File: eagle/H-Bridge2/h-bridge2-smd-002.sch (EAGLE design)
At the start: 29 parts

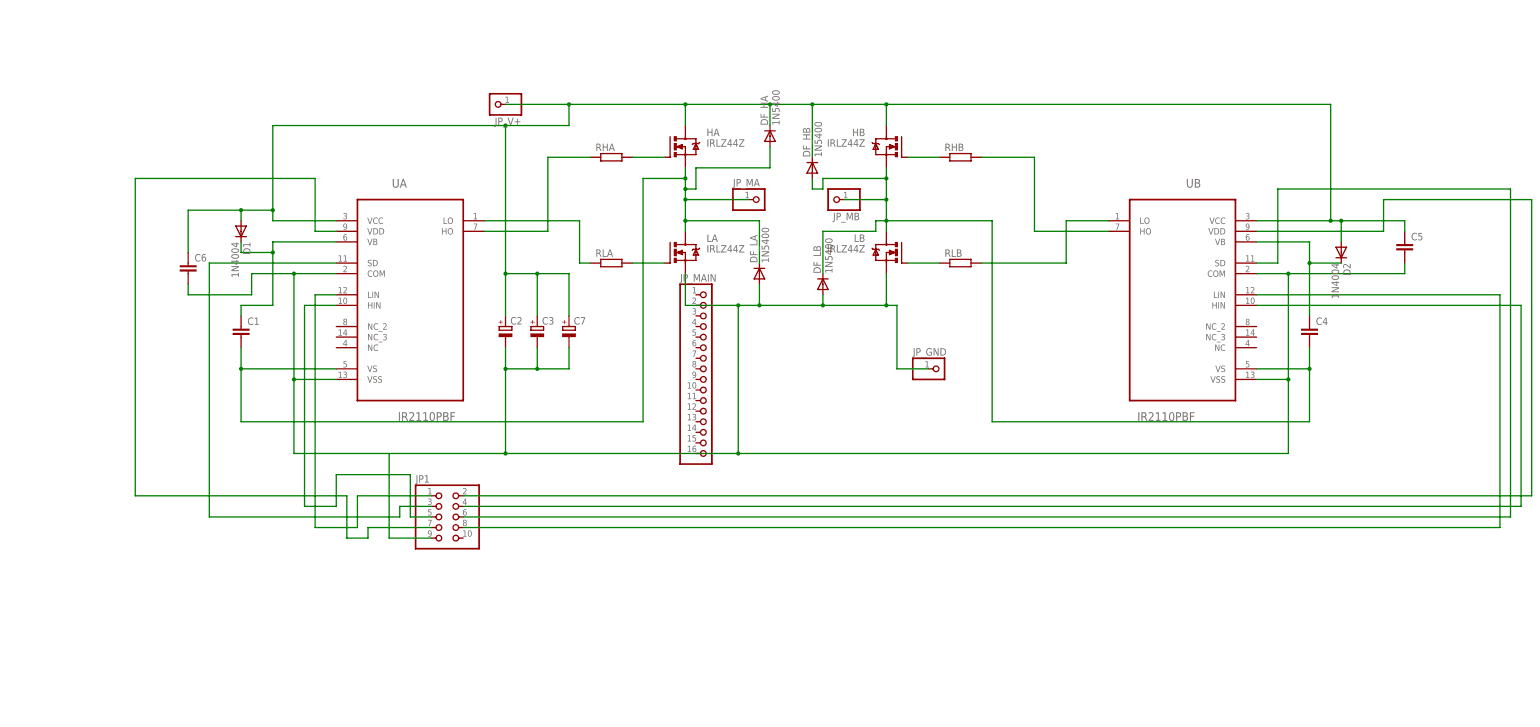
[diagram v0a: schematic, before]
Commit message: eagle merge template board with h-br
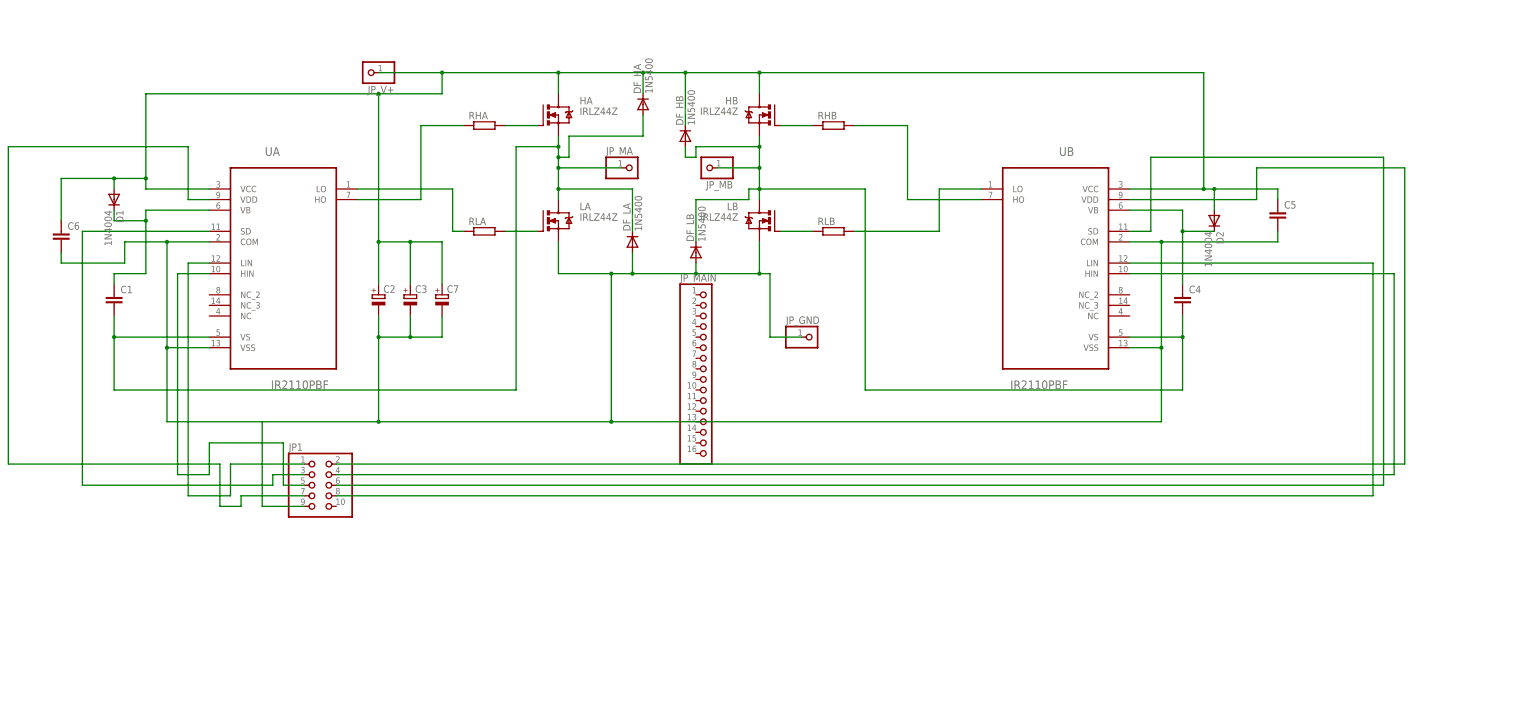
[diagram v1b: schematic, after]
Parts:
- RLA: device rcl:R-EU_0411/15 -> rcl:R-EU_R0603
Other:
- moved on the sheet: C1, C2, C3, C4, C5, C6, C7, D1, D2, DF_HA, DF_HB, DF_LA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

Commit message: H-bridge on SMD
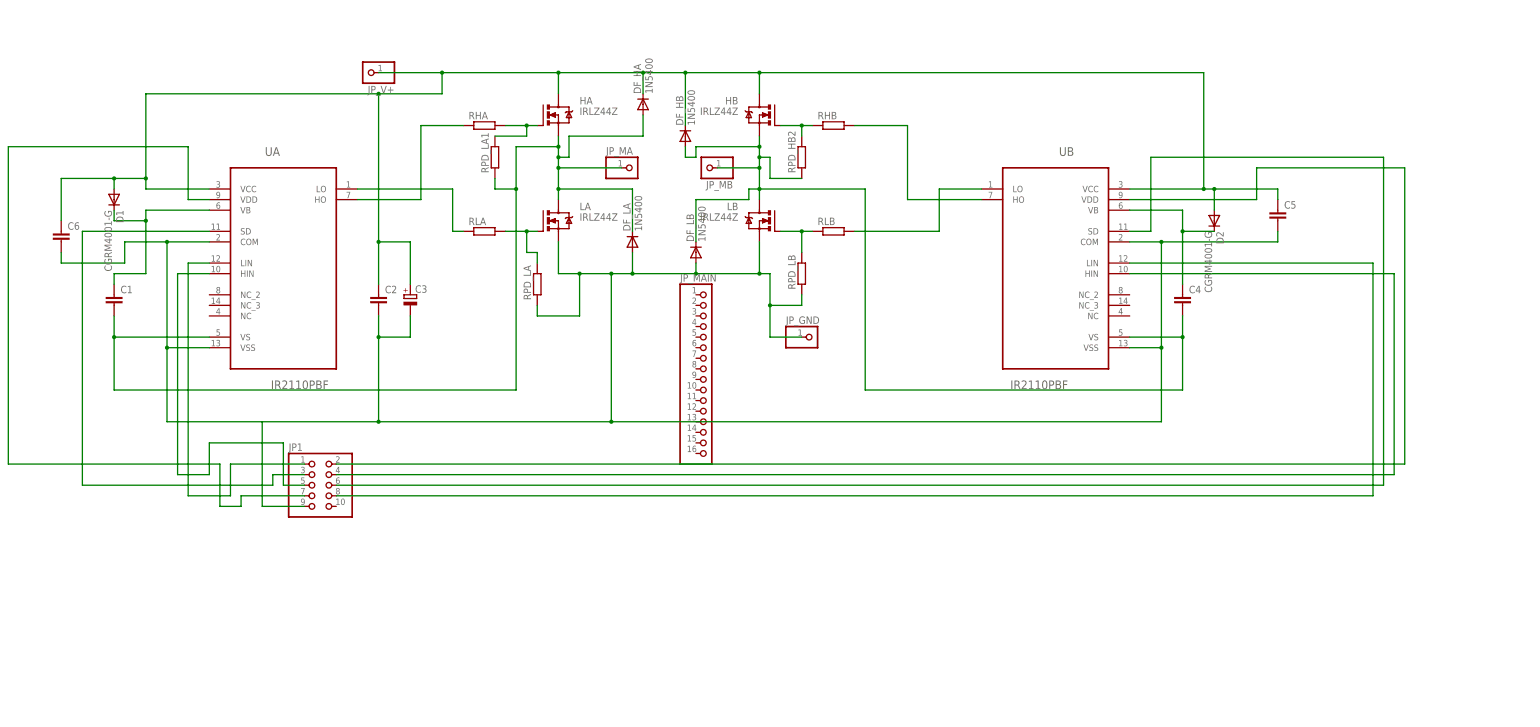
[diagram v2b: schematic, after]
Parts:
- removed C7: (no value), rcl:CPOL-EUE5-13
- added RPD_HB2, RPD_LA, RPD_LA1, RPD_LB: (no value), rcl:R-EU_R1206
- C1, C4, C5, C6: device rcl:C-EU025-025X050 -> rcl:C-EUC4532
- C2: device rcl:CPOL-EUE5-13 -> rcl:C-EU025-024X044
- D1, D2: value 1N4004 -> CGRM4001-G; device diode:1N4004 -> diode:CGRM4001-G
- RHA, RHB, RLB: device rcl:R-EU_0411/15 -> rcl:R-EU_R1206
- RLA: device rcl:R-EU_R0603 -> rcl:R-EU_R1206
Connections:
- net N$13: now also C2.1; no longer C2.+, C7.+
- net N$16: now also RPD_HB2.1
- net N$17: now also RPD_LA1.1
- net N$4: now also C2.2, RPD_LA.1, RPD_LB.1; no longer C2.-, C7.-
- net N$5: now also RPD_LA.2
- net N$6: now also RPD_LA1.2
- net N$7: now also RPD_HB2.2
- net N$8: now also RPD_LB.2

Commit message: H-bridge smd
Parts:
- removed C2: (no value), rcl:C-EU025-024X044
- added C7, C8: (no value), rcl:C-EUC4532
- added C9: (no value), rcl:CPOL-EUE5-13
- added JP_GND1, JP_V+1: (no value), dbg-misc:PINHD-1X1
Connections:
- net N$13: now also C7.1, C8.1, C9.+, JP_V+1.1; no longer C2.1
- net N$4: now also C7.2, C8.2, C9.-, JP_GND1.1; no longer C2.2
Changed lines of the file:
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@@
 <part name="DF_LB" library="dbg-misc" deviceset="1N5400" device=""/>
 <part name="DF_LA" library="dbg-misc" deviceset="1N5400" device=""/>
-<part name="C2" library="rcl" deviceset="C-EU" device="025-024X044"/>
 <part name="C3" library="rcl" deviceset="CPOL-EU" device="E5-13"/>
 <part name="RPD_LB" library="rcl" deviceset="R-EU_" device="R1206"/>
@@
 <part name="RPD_LA1" library="rcl" deviceset="R-EU_" device="R1206"/>
 <part name="RPD_HB2" library="rcl" deviceset="R-EU_" device="R1206"/>
+<part name="C7" library="rcl" deviceset="C-EU" device="C4532"/>
+<part name="C8" library="rcl" deviceset="C-EU" device="C4532"/>
+<part name="C9" library="rcl" deviceset="CPOL-EU" device="E5-13"/>
+<part name="JP_V+1" library="dbg-misc" deviceset="PINHD-1X1" device=""/>
+<part name="JP_GND1" library="dbg-misc" deviceset="PINHD-1X1" device=""/>
 </parts>
 <sheets>
@@
 <instance part="DF_LB" gate="1" x="10.16" y="78.74" rot="R90"/>
 <instance part="DF_LA" gate="1" x="-5.08" y="81.28" rot="R90"/>
-<instance part="C2" gate="G$1" x="-66.04" y="68.58"/>
 <instance part="C3" gate="G$1" x="-58.42" y="68.58"/>
 <instance part="RPD_LB" gate="G$1" x="35.56" y="73.66" rot="R90"/>
@@
 <instance part="RPD_LA1" gate="G$1" x="-38.1" y="101.6" rot="R90"/>
 <instance part="RPD_HB2" gate="G$1" x="35.56" y="101.6" rot="R90"/>
+<instance part="C7" gate="G$1" x="-66.04" y="68.58"/>
+<instance part="C8" gate="G$1" x="-50.8" y="68.58"/>
+<instance part="C9" gate="G$1" x="-43.18" y="68.58"/>
+<instance part="JP_V+1" gate="G$1" x="-68.58" y="134.62" rot="R180"/>
+<instance part="JP_GND1" gate="G$1" x="38.1" y="48.26"/>
 </instances>
 <busses>
@@
 <junction x="10.16" y="73.66"/>
 <junction x="-5.08" y="73.66"/>
-<pinref part="C2" gate="G$1" pin="2"/>
 <wire x1="-66.04" y1="63.5" x2="-66.04" y2="58.42" width="0.1524" layer="91"/>
 <junction x="-66.04" y="38.1"/>
@@
 <wire x1="35.56" y1="66.04" x2="27.94" y2="66.04" width="0.1524" layer="91"/>
 <junction x="27.94" y="66.04"/>
+<pinref part="C7" gate="G$1" pin="2"/>
+<pinref part="C9" gate="G$1" pin="-"/>
+<wire x1="-58.42" y1="58.42" x2="-50.8" y2="58.42" width="0.1524" layer="91"/>
+<wire x1="-50.8" y1="58.42" x2="-43.18" y2="58.42" width="0.1524" layer="91"/>
+<wire x1="-43.18" y1="58.42" x2="-43.18" y2="63.5" width="0.1524" layer="91"/>
+<pinref part="C8" gate="G$1" pin="2"/>
+<wire x1="-50.8" y1="63.5" x2="-50.8" y2="58.42" width="0.1524" layer="91"/>
+<junction x="-50.8" y="58.42"/>
+<pinref part="JP_GND1" gate="G$1" pin="1"/>
+<wire x1="35.56" y1="48.26" x2="27.94" y2="48.26" width="0.1524" layer="91"/>
+<wire x1="27.94" y1="48.26" x2="27.94" y2="58.42" width="0.1524" layer="91"/>
+<junction x="27.94" y="58.42"/>
 </segment>
 </net>
@@
 <wire x1="-66.04" y1="121.92" x2="-50.8" y2="121.92" width="0.1524" layer="91"/>
 <pinref part="HB" gate="G$1" pin="D"/>
-<wire x1="-50.8" y1="121.92" x2="-22.86" y2="121.92" width="0.1524" layer="91"/>
+<wire x1="-50.8" y1="121.92" x2="-43.18" y2="121.92" width="0.1524" layer="91"/>
+<wire x1="-43.18" y1="121.92" x2="-22.86" y2="121.92" width="0.1524" layer="91"/>
 <wire x1="-22.86" y1="121.92" x2="-2.54" y2="121.92" width="0.1524" layer="91"/>
 <wire x1="-2.54" y1="121.92" x2="7.62" y2="121.92" width="0.1524" layer="91"/>
@@
 <junction x="-2.54" y="121.92"/>
 <junction x="7.62" y="121.92"/>
-<pinref part="C2" gate="G$1" pin="1"/>
 <wire x1="-66.04" y1="116.84" x2="-66.04" y2="81.28" width="0.1524" layer="91"/>
 <junction x="-66.04" y="116.84"/>
@@
 <wire x1="-58.42" y1="81.28" x2="-58.42" y2="71.12" width="0.1524" layer="91"/>
 <junction x="-66.04" y="81.28"/>
-</segment>
-</net>
+<pinref part="C7" gate="G$1" pin="1"/>
+<pinref part="C9" gate="G$1" pin="+"/>
+<wire x1="-58.42" y1="81.28" x2="-50.8" y2="81.28" width="0.1524" layer="91"/>
+<wire x1="-50.8" y1="81.28" x2="-43.18" y2="81.28" width="0.1524" layer="91"/>
+<wire x1="-43.18" y1="81.28" x2="-43.18" y2="71.12" width="0.1524" layer="91"/>
+<pinref part="C8" gate="G$1" pin="1"/>
+<wire x1="-50.8" y1="81.28" x2="-50.8" y2="71.12" width="0.1524" layer="91"/>
+<junction x="-58.42" y="81.28"/>
+<junction x="-50.8" y="81.28"/>
+<pinref part="JP_V+1" gate="G$1" pin="1"/>
+<wire x1="-66.04" y1="134.62" x2="-43.18" y2="134.62" width="0.1524" layer="91"/>
+<wire x1="-43.18" y1="134.62" x2="-43.18" y2="121.92" width="0.1524" layer="91"/>
+</segment>
+</net>
